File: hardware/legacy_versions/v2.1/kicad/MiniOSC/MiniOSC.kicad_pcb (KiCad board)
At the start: 2 copper layers, 65 x 128.5 mm, 82 parts, among them J1 SYNC_IN, J10 FM_IN, J11 PWM_CV, J12 TRI_OUT, J13 SAW_OUT, J14 PULSE_OUT, J2 Conn_01x10_Pin, J9 VOCT_IN, Q1 BC549, Q2 BC559, SW1 SW_DPDT_x2, U1 40106, U2 TL074, U3 TL074

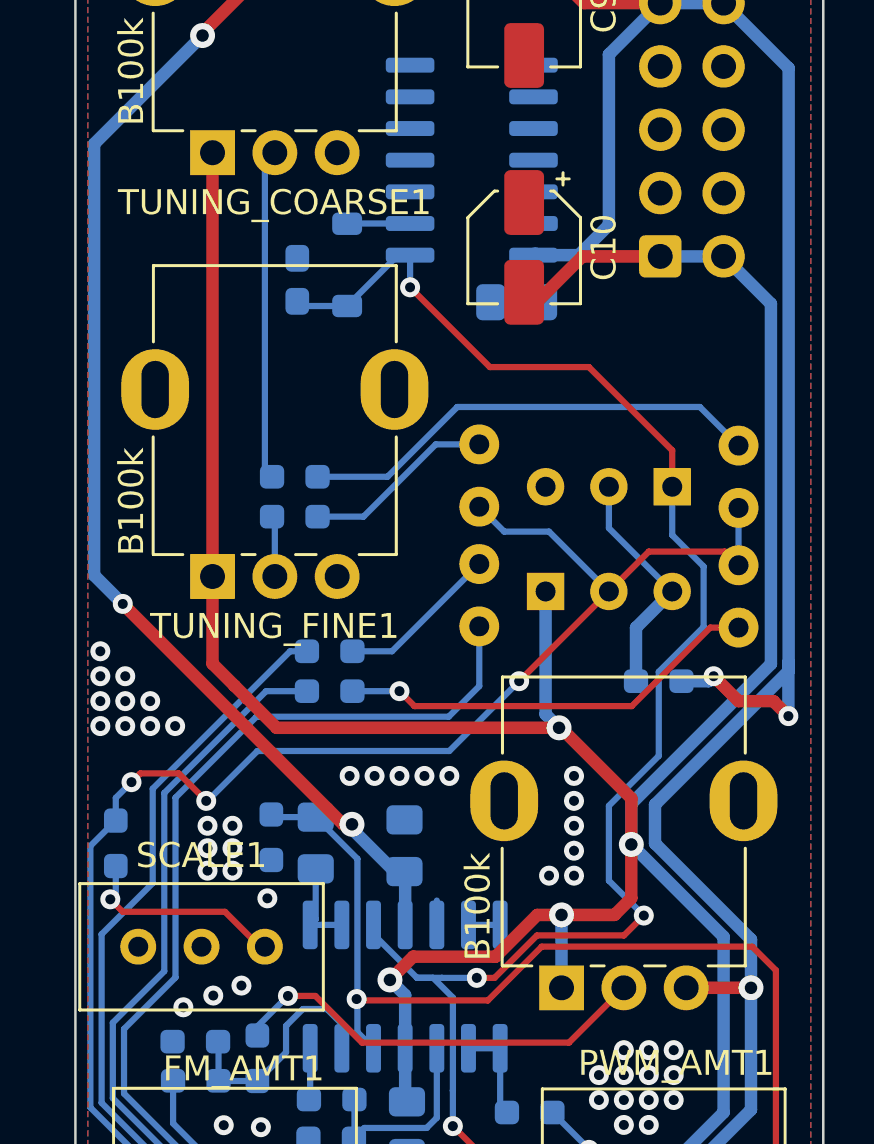
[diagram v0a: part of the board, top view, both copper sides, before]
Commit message: Test PCB for v2.1.1 with throughole parts
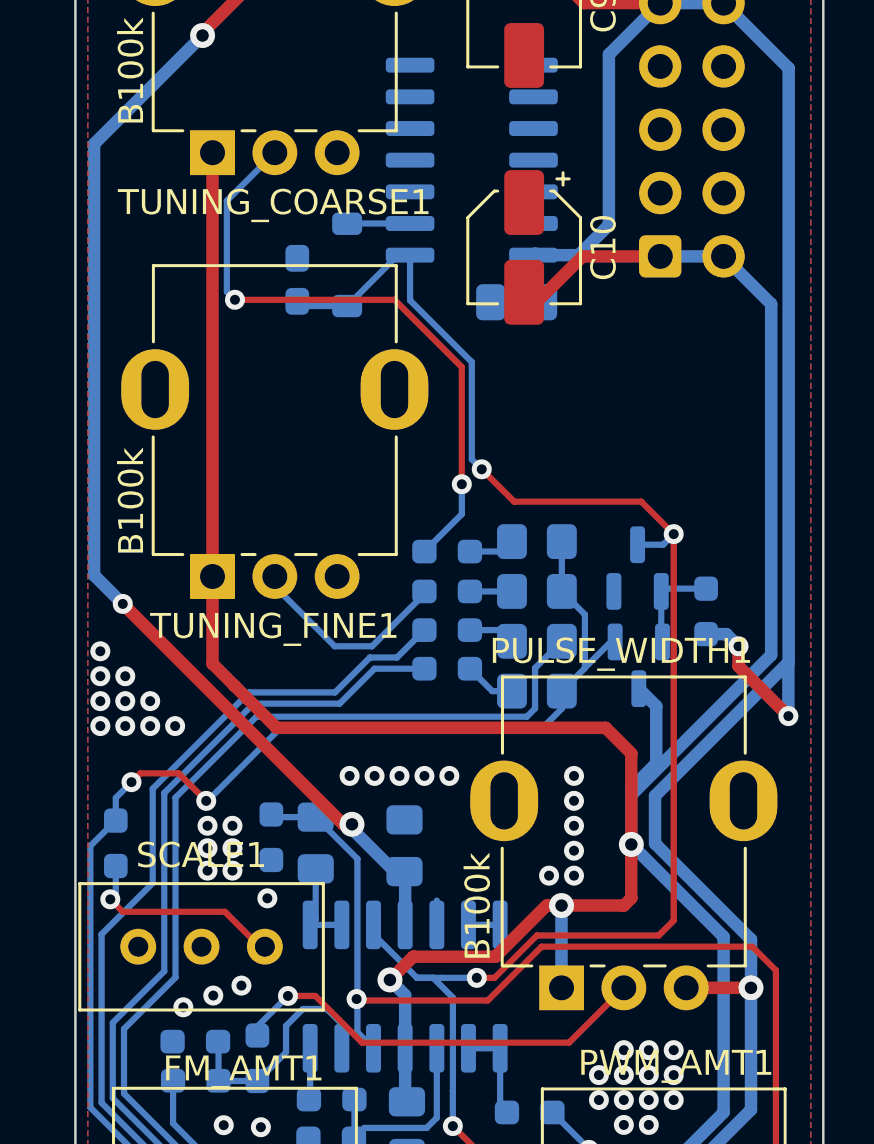
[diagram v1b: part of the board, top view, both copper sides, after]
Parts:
- removed Q1: BC549, Package_TO_SOT_THT:TO-92_Inline_Wide
- removed Q2: BC559, Package_TO_SOT_THT:TO-92_Inline_Wide
- added Q3: BC848, Package_TO_SOT_SMD:SOT-23, B.Cu at (197.6, 78.7)
- added Q4: BC858, Package_TO_SOT_SMD:SOT-23, B.Cu at (197.6, 82.6)
- TH1, TH2, TH3, TH4: footprint Capacitor_THT:C_Disc_D3.8mm_W2.6mm_P2.50mm -> Resistor_SMD:R_0805_2012Metric_Pad1.20x1.40mm_HandSolder
- moved TH4 9.53 mm to (193.5, 83.6), turned to 180 degrees
- moved TH2 8.20 mm to (193.5, 77.6), turned to 180 degrees
- moved R3 6.81 mm to (189.9, 79.6)
- moved R4 6.81 mm to (189.9, 78.0)
- moved R2 4.80 mm to (189.9, 82.7)
- moved R1 4.79 mm to (189.9, 81.2)
- moved TH3 4.11 mm to (193.5, 79.6), turned to 180 degrees
- moved R6 3.38 mm to (200.3, 80.4), turned to -90 degrees
- moved TH1 2.39 mm to (193.5, 81.6), turned to 180 degrees
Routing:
- net Net-(R4-Pad1): track 18.7 -> 1.85 mm
- net Net-(R2-Pad1): track 17.0 -> 2.06 mm, vias 1 -> 0
- net Net-(R4-Pad2): track 13.3 -> 25.1 mm, vias 0 -> 2
- net Net-(Q4-B): track 69.3 -> 59.6 mm, vias 3 -> 2
- net Net-(R3-Pad1): track 7.69 -> 1.69 mm
- net Net-(R3-Pad2): track 2.45 -> 8.36 mm
- net Net-(Q3-B): track 9.45 -> 3.89 mm
- net Net-(J9-PadT): track 70.7 -> 75.8 mm
- net Net-(J10-PadT): track 56.7 -> 61.8 mm
- net Net-(R1-Pad1): track 6.54 -> 1.87 mm
- net Net-(FM_AMT1-Pad3): track 51.3 -> 53.9 mm
- net Net-(D3-K): track 116.3 -> 117.3 mm
- net -12V: track 184.1 -> 184.8 mm, vias 6 -> 5
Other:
- board text added: "MiniOSC v2.1"
- board text removed: "MiniOSC v2.1.1"
